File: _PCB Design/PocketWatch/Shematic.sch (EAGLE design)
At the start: 43 parts, among them Q1 MMBTA56-SOT23, U2 ATTINY88-AU

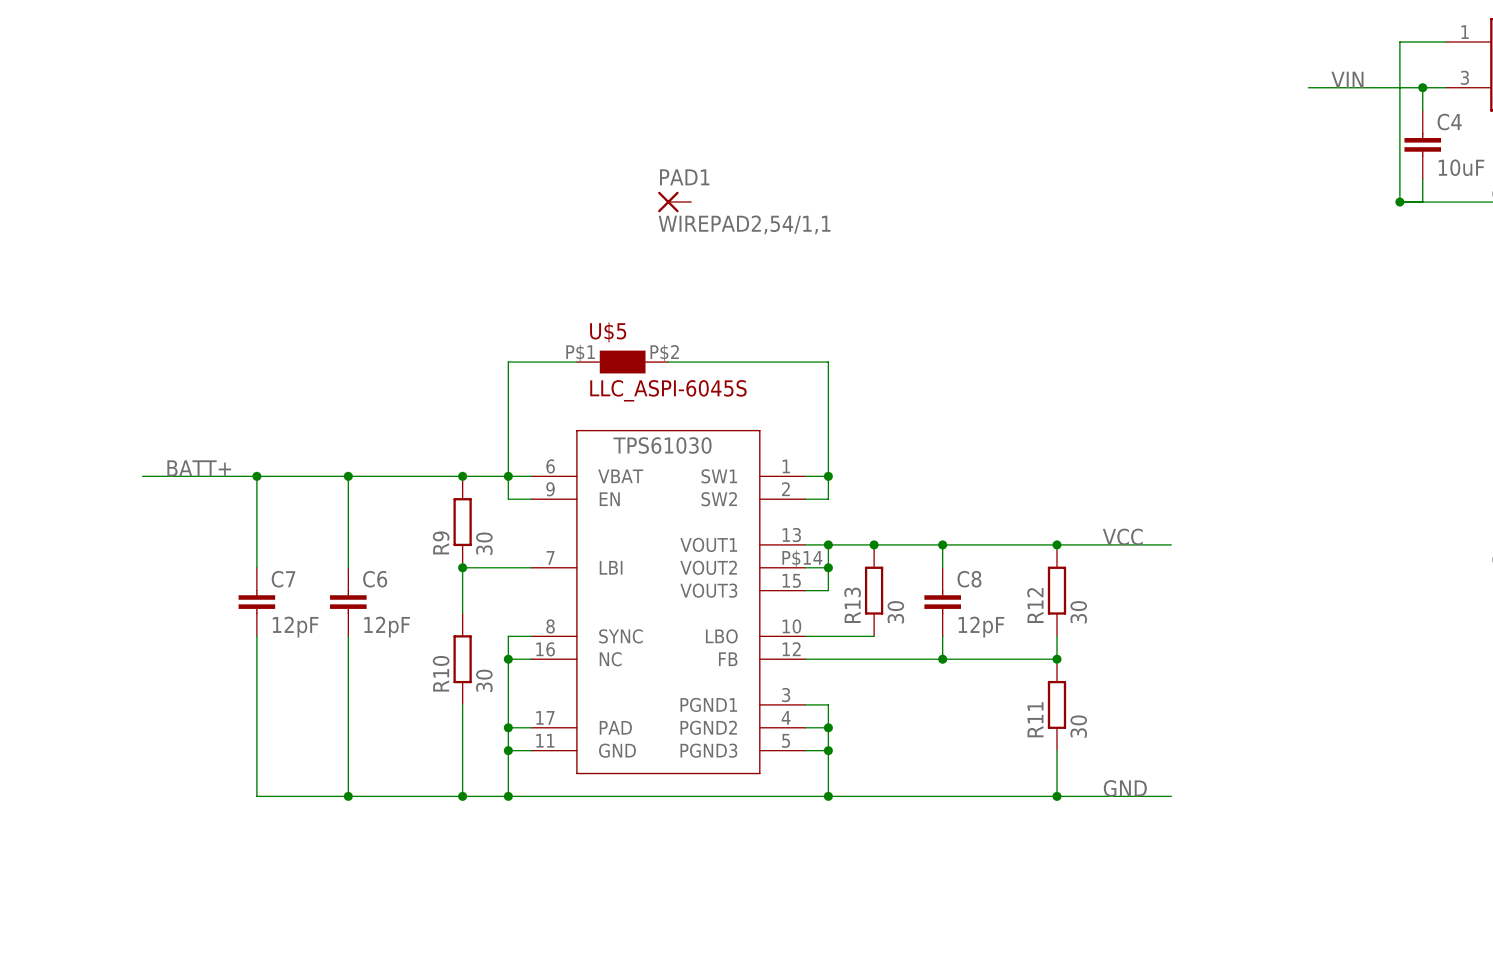
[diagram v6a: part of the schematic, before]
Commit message: Completed Boost Circuitry. Slight modifications
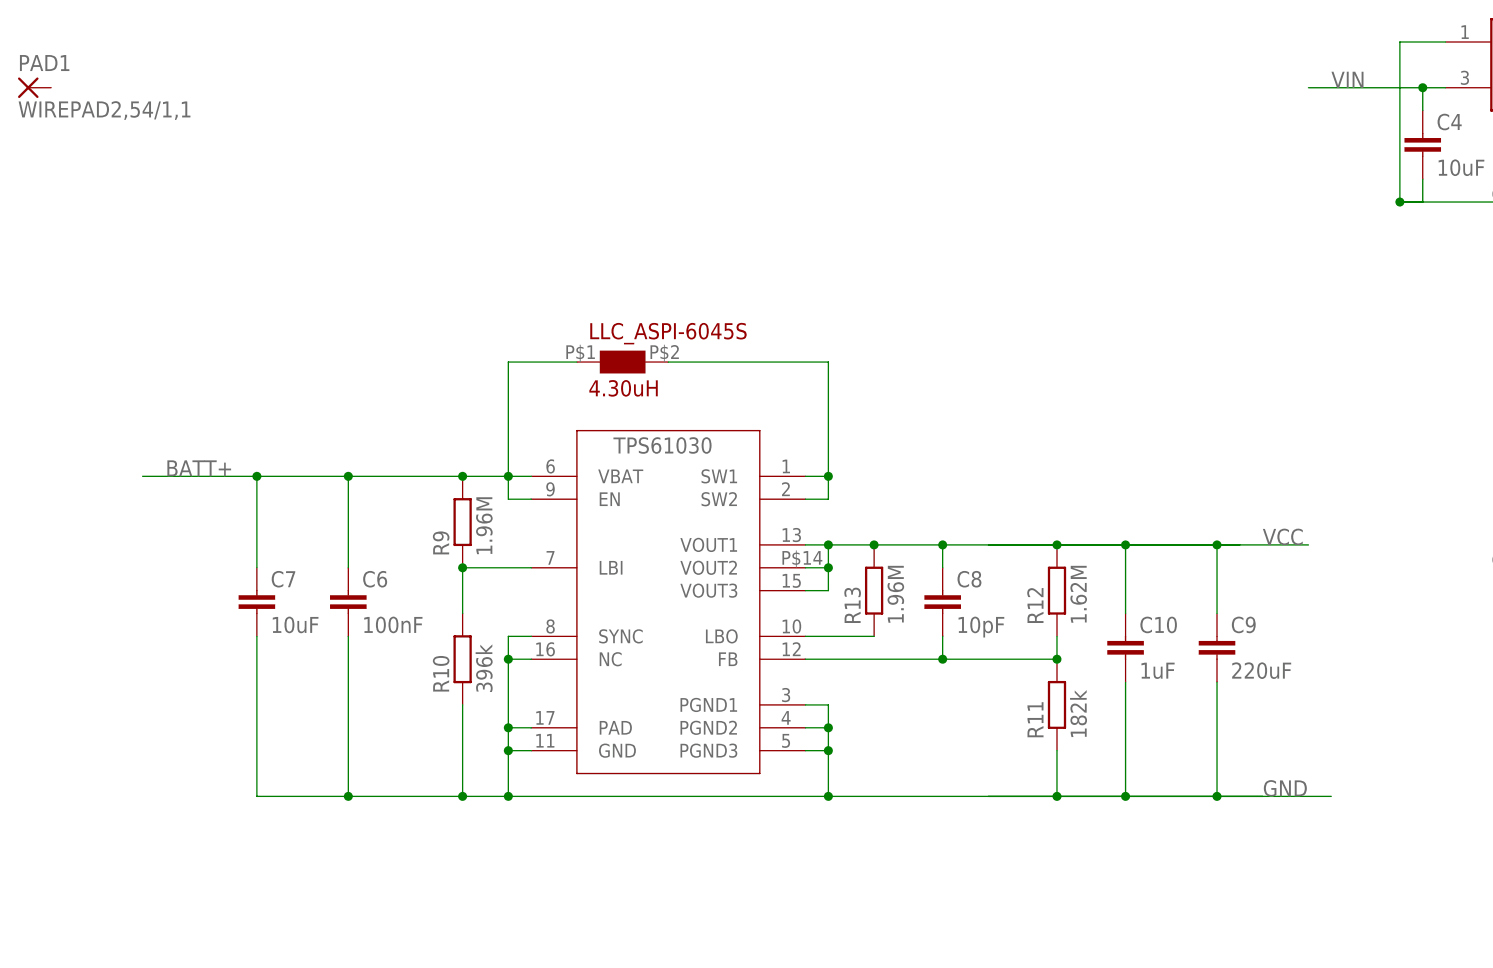
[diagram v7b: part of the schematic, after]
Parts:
- added C10: 1uF, eagle-ltspice:CC1206
- added C9: 220uF, eagle-ltspice:CC1206
- C6: value 12pF -> 100nF
- C7: value 12pF -> 10uF
- C8: value 12pF -> 10pF
- LLC_ASPI-6045S: value LLC_ASPI-6045S -> 4.30uH
- R10: value 30 -> 396k
- R11: value 30 -> 182k
- R12: value 30 -> 1.62M
- R13, R9: value 30 -> 1.96M
- renumbered U$5 to LLC_ASPI-6045S
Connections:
- new net GND1: C10.2
- new net VCC1: C10.1
- net GND: now also C9.2
- net VCC: now also C9.1
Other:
- moved on the sheet: PAD1
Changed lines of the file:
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@@
 <part name="R7" library="eagle-ltspice" library_urn="urn:adsk.eagle:library:217" deviceset="R" device="R1206" package3d_urn="urn:adsk.eagle:package:13301/1" value="30"/>
 <part name="R8" library="eagle-ltspice" library_urn="urn:adsk.eagle:library:217" deviceset="R" device="R1206" package3d_urn="urn:adsk.eagle:package:13301/1" value="30"/>
-<part name="C6" library="eagle-ltspice" library_urn="urn:adsk.eagle:library:217" deviceset="C" device="C1206" package3d_urn="urn:adsk.eagle:package:13279/1" value="12pF"/>
-<part name="C7" library="eagle-ltspice" library_urn="urn:adsk.eagle:library:217" deviceset="C" device="C1206" package3d_urn="urn:adsk.eagle:package:13279/1" value="12pF"/>
-<part name="R9" library="eagle-ltspice" library_urn="urn:adsk.eagle:library:217" deviceset="R" device="R1206" package3d_urn="urn:adsk.eagle:package:13301/1" value="30"/>
-<part name="R10" library="eagle-ltspice" library_urn="urn:adsk.eagle:library:217" deviceset="R" device="R1206" package3d_urn="urn:adsk.eagle:package:13301/1" value="30"/>
-<part name="C8" library="eagle-ltspice" library_urn="urn:adsk.eagle:library:217" deviceset="C" device="C1206" package3d_urn="urn:adsk.eagle:package:13279/1" value="12pF"/>
-<part name="R11" library="eagle-ltspice" library_urn="urn:adsk.eagle:library:217" deviceset="R" device="R1206" package3d_urn="urn:adsk.eagle:package:13301/1" value="30"/>
-<part name="R12" library="eagle-ltspice" library_urn="urn:adsk.eagle:library:217" deviceset="R" device="R1206" package3d_urn="urn:adsk.eagle:package:13301/1" value="30"/>
-<part name="R13" library="eagle-ltspice" library_urn="urn:adsk.eagle:library:217" deviceset="R" device="R1206" package3d_urn="urn:adsk.eagle:package:13301/1" value="30"/>
-<part name="U$5" library="Library" deviceset="LLC_ASPI-6045S" device=""/>
+<part name="C6" library="eagle-ltspice" library_urn="urn:adsk.eagle:library:217" deviceset="C" device="C1206" package3d_urn="urn:adsk.eagle:package:13279/1" value="100nF"/>
+<part name="C7" library="eagle-ltspice" library_urn="urn:adsk.eagle:library:217" deviceset="C" device="C1206" package3d_urn="urn:adsk.eagle:package:13279/1" value="10uF"/>
+<part name="R9" library="eagle-ltspice" library_urn="urn:adsk.eagle:library:217" deviceset="R" device="R1206" package3d_urn="urn:adsk.eagle:package:13301/1" value="1.96M"/>
+<part name="R10" library="eagle-ltspice" library_urn="urn:adsk.eagle:library:217" deviceset="R" device="R1206" package3d_urn="urn:adsk.eagle:package:13301/1" value="396k"/>
+<part name="C8" library="eagle-ltspice" library_urn="urn:adsk.eagle:library:217" deviceset="C" device="C1206" package3d_urn="urn:adsk.eagle:package:13279/1" value="10pF"/>
+<part name="R11" library="eagle-ltspice" library_urn="urn:adsk.eagle:library:217" deviceset="R" device="R1206" package3d_urn="urn:adsk.eagle:package:13301/1" value="182k"/>
+<part name="R12" library="eagle-ltspice" library_urn="urn:adsk.eagle:library:217" deviceset="R" device="R1206" package3d_urn="urn:adsk.eagle:package:13301/1" value="1.62M"/>
+<part name="R13" library="eagle-ltspice" library_urn="urn:adsk.eagle:library:217" deviceset="R" device="R1206" package3d_urn="urn:adsk.eagle:package:13301/1" value="1.96M"/>
+<part name="LLC_ASPI-6045S" library="Library" deviceset="LLC_ASPI-6045S" device="" value="4.30uH"/>
 <part name="U$6" library="Library" deviceset="TPS61030" device=""/>
+<part name="C9" library="eagle-ltspice" library_urn="urn:adsk.eagle:library:217" deviceset="C" device="C1206" package3d_urn="urn:adsk.eagle:package:13279/1" value="220uF"/>
+<part name="C10" library="eagle-ltspice" library_urn="urn:adsk.eagle:library:217" deviceset="C" device="C1206" package3d_urn="urn:adsk.eagle:package:13279/1" value="1uF"/>
 </parts>
 <sheets>
@@
 <instance part="C4" gate="G$1" x="0" y="101.6"/>
 <instance part="C5" gate="G$1" x="22.86" y="101.6"/>
-<instance part="PAD1" gate="G$1" x="-83.82" y="93.98"/>
+<instance part="PAD1" gate="G$1" x="-154.94" y="106.68"/>
 <instance part="SV1" gate="1" x="124.46" y="10.16" rot="R180"/>
 <instance part="SV3" gate="1" x="162.56" y="20.32"/>
@@
 <instance part="R12" gate="G$1" x="-40.64" y="50.8" rot="R90"/>
 <instance part="R13" gate="G$1" x="-60.96" y="50.8" rot="R90"/>
-<instance part="U$5" gate="G$1" x="-88.9" y="76.2"/>
+<instance part="LLC_ASPI-6045S" gate="G$1" x="-88.9" y="76.2"/>
 <instance part="U$6" gate="G$1" x="-83.82" y="55.88"/>
+<instance part="C9" gate="G$1" x="-22.86" y="45.72"/>
+<instance part="C10" gate="G$1" x="-33.02" y="45.72"/>
 </instances>
 <busses>
@@
 <wire x1="-129.54" y1="27.94" x2="-129.54" y2="45.72" width="0.1524" layer="91"/>
 <junction x="-119.38" y="27.94"/>
-<wire x1="-40.64" y1="27.94" x2="-27.94" y2="27.94" width="0.1524" layer="91"/>
+<wire x1="-40.64" y1="27.94" x2="-22.86" y2="27.94" width="0.1524" layer="91"/>
 <junction x="-40.64" y="27.94"/>
-<label x="-35.56" y="27.94" size="1.778" layer="95"/>
+<label x="-17.78" y="27.94" size="1.778" layer="95"/>
+<pinref part="C9" gate="G$1" pin="2"/>
+<wire x1="-22.86" y1="27.94" x2="-10.16" y2="27.94" width="0.1524" layer="91"/>
+<wire x1="-22.86" y1="40.64" x2="-22.86" y2="27.94" width="0.1524" layer="91"/>
+<junction x="-22.86" y="27.94"/>
 </segment>
 </net>
@@
 <wire x1="-53.34" y1="55.88" x2="-53.34" y2="53.34" width="0.1524" layer="91"/>
 <junction x="-53.34" y="55.88"/>
-<wire x1="-40.64" y1="55.88" x2="-27.94" y2="55.88" width="0.1524" layer="91"/>
+<wire x1="-40.64" y1="55.88" x2="-22.86" y2="55.88" width="0.1524" layer="91"/>
 <junction x="-40.64" y="55.88"/>
-<label x="-35.56" y="55.88" size="1.778" layer="95"/>
+<label x="-17.78" y="55.88" size="1.778" layer="95"/>
+<pinref part="C9" gate="G$1" pin="1"/>
+<wire x1="-22.86" y1="55.88" x2="-12.7" y2="55.88" width="0.1524" layer="91"/>
+<wire x1="-22.86" y1="48.26" x2="-22.86" y2="55.88" width="0.1524" layer="91"/>
+<junction x="-22.86" y="55.88"/>
 </segment>
 </net>
@@
 <pinref part="U$6" gate="G$1" pin="VBAT"/>
 <wire x1="-101.6" y1="63.5" x2="-99.06" y2="63.5" width="0.1524" layer="91"/>
-<pinref part="U$5" gate="G$1" pin="P$1"/>
+<pinref part="LLC_ASPI-6045S" gate="G$1" pin="P$1"/>
 <wire x1="-93.98" y1="76.2" x2="-101.6" y2="76.2" width="0.1524" layer="91"/>
 <wire x1="-101.6" y1="76.2" x2="-101.6" y2="63.5" width="0.1524" layer="91"/>
@@
 <pinref part="U$6" gate="G$1" pin="SW1"/>
 <wire x1="-66.04" y1="63.5" x2="-68.58" y2="63.5" width="0.1524" layer="91"/>
-<pinref part="U$5" gate="G$1" pin="P$2"/>
+<pinref part="LLC_ASPI-6045S" gate="G$1" pin="P$2"/>
 <wire x1="-66.04" y1="63.5" x2="-66.04" y2="76.2" width="0.1524" layer="91"/>
 <wire x1="-66.04" y1="76.2" x2="-83.82" y2="76.2" width="0.1524" layer="91"/>
@@
 </segment>
 </net>
+<net name="GND1" class="0">
+<segment>
+<wire x1="-48.26" y1="27.94" x2="-33.02" y2="27.94" width="0.1524" layer="91"/>
+<pinref part="C10" gate="G$1" pin="2"/>
+<wire x1="-33.02" y1="27.94" x2="-17.78" y2="27.94" width="0.1524" layer="91"/>
+<wire x1="-33.02" y1="40.64" x2="-33.02" y2="27.94" width="0.1524" layer="91"/>
+<junction x="-33.02" y="27.94"/>
+</segment>
+</net>
+<net name="VCC1" class="0">
+<segment>
+<wire x1="-48.26" y1="55.88" x2="-33.02" y2="55.88" width="0.1524" layer="91"/>
+<pinref part="C10" gate="G$1" pin="1"/>
+<wire x1="-33.02" y1="55.88" x2="-20.32" y2="55.88" width="0.1524" layer="91"/>
+<wire x1="-33.02" y1="48.26" x2="-33.02" y2="55.88" width="0.1524" layer="91"/>
+<junction x="-33.02" y="55.88"/>
+</segment>
+</net>

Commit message: Added LEDs, added switch connectors, Various Fixes
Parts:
- removed C4, C5: 10uF, eagle-ltspice:CC1206
- removed NCP1117: DPAK, smd-footprints:DPAK
- removed SV4: (no value), con-lstb:MA04-1
- added AM, COLIN1, COLIN2, PM: (no value), eagle-ltspice:LED_E
- added PAD2, PAD3: WIREPAD2,54/1,1, wirepad:WIREPAD2,54/1,1
- added PAD4, PAD5, PAD6: WIREPAD, wirepad:WIREPAD2,54/1,1
- added R14, R15, R16, R17: 1k, eagle-ltspice:RR1206
- added R18, R19, R20: 10k, eagle-ltspice:RR1206
- R2: value 2k -> 10k
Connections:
- removed net GND1: C10.2
- removed net TG4: T4.C
- removed net VCC1: C10.1
- removed net VIN: C4.1, NCP1117.P$3
- new net B_DOWN: PAD6.P, R20.1, U2.PC2_(ADC2/PCINT10)
- new net B_SEL: PAD4.P, R18.1, U2.PC0_(ADC0/PCINT8)
- new net B_UP: PAD5.P, R19.1, U2.PC1_(ADC1/PCINT9)
- new net COIN: MCP7940M.P$8
- new net N$12: AM.A, R16.1
- new net N$14: PM.A, R17.1
- new net N$15: R14.2, R15.2, U2.PB0_(PCINT0/CLKO/ICP1)
- new net N$16: R17.2, U2.PB2_(PCINT2/!SS!/OC1B)
- new net N$17: R16.2, U2.PB1_(PCINT1/OC1A)
- new net N$7: COLIN1.A, R14.1
- new net N$9: COLIN2.A, R15.1
- net BATT+: now also PAD1.P
- net EN0: no longer SV4.4
- net EN1: no longer SV4.3
- net EN2: no longer SV4.2
- net EN3: no longer SV4.1
- net GND: now also AM.C, C10.2, COLIN1.C, COLIN2.C, PAD3.P, PM.C; no longer C4.2, C5.2, NCP1117.P$1
- net MFP: now also U2.PC3_(ADC3/PCINT11); no longer U2.PC2_(ADC2/PCINT10)
- net TG2: now also T3.C
- net TG3: now also T4.C; no longer T3.C
- net VCC: now also C10.1, PAD2.P, R18.2, R19.2, R20.2; no longer C5.1, MCP7940M.P$8, NCP1117.P$2
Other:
- moved on the sheet: PAD1, R5, R6, R7, R8, SV5, SV6, T1, T2, T3, T4
